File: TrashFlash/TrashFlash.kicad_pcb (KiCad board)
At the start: 2 copper layers, 105 x 45 mm, 113 parts, among them IC1 LTC3643IUDD#PBF, IC10 BQ24230RGTR, IC11 STM32L471QEI6, IC2 ADG5419BCPZ-RL7, IC3 BQ27426YZFR, IC4 SN74LXC2T45QDTTRQ1, IC5 TPS63900DSKR, IC6 TPS63900DSKR, IC7 LP5024RSMR, IC8 AD8615AUJZ-REEL, IC9 BQ29732DSER, J1 USB4800-03-A, Q1 BC56-10PA,115, Q2 BC56-10PA,115, Q3 BC56-10PA,115, Q4 BC56-10PA,115, Q5 PMDPB30XNAX, U1 SI5448DU-T1-GE3, U2 SI5448DU-T1-GE3, Y1 ECS-160-8-33B2-CTN-TR3

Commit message: Added Wireless and inter PCB connector
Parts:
- removed LED1, LED2, LED3, LED4, LED5, LED6, LED7, LED8: 150353M153300, TrashFlash:150353M153300
- added ANT801: 0868AT43A0020001E, TrashFlash:ANTC7020X90N, F.Cu at (276.5, 102.4)
- added C201: 100p, Capacitor_SMD:C_0402_1005Metric, F.Cu at (40.2, 79.1)
- added C202: 100p, Capacitor_SMD:C_0402_1005Metric, F.Cu at (40.2, 81.1)
- added C304: 10u, Capacitor_SMD:C_1206_3216Metric, F.Cu at (40.5, 188.2)
- added C305: 10u, Capacitor_SMD:C_1206_3216Metric, F.Cu at (40.5, 191.5)
- added C801: 1.5p, Capacitor_SMD:C_0402_1005Metric, F.Cu at (264.4, 101.3)
- added C802: 1p, Capacitor_SMD:C_0402_1005Metric, F.Cu at (264.4, 103.3)
- added C803: 100p, Capacitor_SMD:C_0402_1005Metric, F.Cu at (264.4, 105.3)
- added C804: 1.5p, Capacitor_SMD:C_0402_1005Metric, F.Cu at (264.4, 107.2)
- added C805: 3.3p, Capacitor_SMD:C_0402_1005Metric, F.Cu at (264.4, 109.2)
- added C806: 3.9p, Capacitor_SMD:C_0402_1005Metric, F.Cu at (264.4, 111.2)
- added C807: 0.3p, Capacitor_SMD:C_0402_1005Metric, F.Cu at (264.4, 113.2)
- added C808: 10p, Capacitor_SMD:C_0402_1005Metric, F.Cu at (267.2, 101.3)
- added C809: 10p, Capacitor_SMD:C_0402_1005Metric, F.Cu at (267.2, 103.3)
- added C810: 100p, Capacitor_SMD:C_0402_1005Metric, F.Cu at (267.2, 105.3)
- added C811: 100n, Capacitor_SMD:C_0402_1005Metric, F.Cu at (267.2, 107.2)
- added C812: 220p, Capacitor_SMD:C_0402_1005Metric, F.Cu at (267.2, 109.2)
- added C813: 220p, Capacitor_SMD:C_0402_1005Metric, F.Cu at (267.2, 111.2)
- added C814: 10n, Capacitor_SMD:C_0402_1005Metric, F.Cu at (267.2, 113.2)
- added C815: 220p, Capacitor_SMD:C_0402_1005Metric, F.Cu at (270.1, 101.3)
- added C816: 10n, Capacitor_SMD:C_0402_1005Metric, F.Cu at (270.1, 103.3)
- added C817: 100n, Capacitor_SMD:C_0402_1005Metric, F.Cu at (270.1, 105.3)
- added IC801: CC110LRGPR, TrashFlash:QFN50P400X400X100-21N-D, F.Cu at (277.0, 113.8)
- added J101: 15130322601000, TrashFlash:15130322601000, B.Cu at (202.0, 125.0)
- added J102: 15230322601000, TrashFlash:15230322601000, F.Cu at (142.0, 126.0)
- added L801: 12n, Inductor_SMD:L_01005_0402Metric, F.Cu at (272.7, 105.3)
- added L802: 18n, Inductor_SMD:L_01005_0402Metric, F.Cu at (272.7, 107.0)
- added L803: 12n, Inductor_SMD:L_01005_0402Metric, F.Cu at (272.7, 108.6)
- added L804: 12n, Inductor_SMD:L_01005_0402Metric, F.Cu at (272.7, 110.3)
- added L805: 18n, Inductor_SMD:L_01005_0402Metric, F.Cu at (272.7, 111.9)
- added L806: 12n, Inductor_SMD:L_01005_0402Metric, F.Cu at (272.7, 113.6)
- added L807: 18n, Inductor_SMD:L_01005_0402Metric, F.Cu at (272.7, 115.2)
- added LED601: 150282M153310, TrashFlash:150282M153310, F.Cu at (185.0, 155.0)
- added LED602: 150282M153310, TrashFlash:150282M153310, F.Cu at (184.5, 150.5)
- added LED603: 150282M153310, TrashFlash:150282M153310, F.Cu at (183.0, 146.3)
- added LED604: 150282M153310, TrashFlash:150282M153310, F.Cu at (180.6, 142.5)
- added LED605: 150282M153310, TrashFlash:150282M153310, F.Cu at (177.5, 139.4)
- added LED606: 150282M153310, TrashFlash:150282M153310, F.Cu at (173.7, 137.0)
- added LED607: 150282M153310, TrashFlash:150282M153310, F.Cu at (169.5, 135.5)
- added LED608: 150282M153310, TrashFlash:150282M153310, F.Cu at (165.0, 135.0)
- added R201: 100k, Resistor_SMD:R_0402_1005Metric, F.Cu at (37.3, 79.1)
- added R202: 5.1k, Resistor_SMD:R_0402_1005Metric, F.Cu at (37.3, 81.1)
- added R203: 100k, Resistor_SMD:R_0402_1005Metric, F.Cu at (37.3, 83.1)
- added R204: 5.1k, Resistor_SMD:R_0402_1005Metric, F.Cu at (37.3, 85.1)
- added R801: 330, Capacitor_SMD:C_0402_1005Metric, F.Cu at (270.1, 107.2)
- added R802: 56k, Capacitor_SMD:C_0402_1005Metric, F.Cu at (270.1, 109.2)
- added Y801: ECS-260-10-33B-CKM-TR, TrashFlash:ECS160833B2CTNTR3, F.Cu at (277.1, 107.5)
- C303: renamed from C7; value 22u -> 10u; footprint Capacitor_SMD:C_0603_1608Metric -> Capacitor_SMD:C_1206_3216Metric
- D201: renamed from D4; moved to B.Cu
- D202: renamed from D3; moved to B.Cu
- D203: renamed from D2; moved to B.Cu
- D204: renamed from D1; moved to B.Cu
- R205: renamed from R9; value 150k -> 100k
- R206: renamed from R7; value 12k -> 10k
- R211: renamed from R6; value 12k -> 10k
- R212: renamed from R8; value 150k -> 100k
- R213: renamed from R18; footprint Resistor_SMD:R_0603_1608Metric -> Resistor_SMD:R_0805_2012Metric
- R214: renamed from R5; footprint Resistor_SMD:R_0603_1608Metric -> Resistor_SMD:R_0805_2012Metric
- R502: renamed from R23; value 36.5k -> 6.49k
- moved Y401 181.7 mm to (275.3, 128.5)
- moved IC401 171.3 mm to (266.7, 126.2)
- moved IC601 162.3 mm to (265.0, 159.0)
- moved C601 155.9 mm to (276.7, 157.4)
- moved C602 155.9 mm to (276.7, 159.9)
- moved R601 155.9 mm to (273.2, 159.1)
- moved R602 155.9 mm to (273.2, 157.2)
- moved R603 155.9 mm to (273.2, 161.1)
- moved C401 139.6 mm to (273.9, 141.2)
- moved C402 139.6 mm to (267.6, 146.3)
- moved C403 139.6 mm to (273.9, 143.7)
- moved C406 139.6 mm to (273.9, 138.7)
- moved C408 139.6 mm to (264.7, 148.3)
- moved C412 139.6 mm to (264.7, 146.3)
- moved C404 139.6 mm to (264.7, 140.4)
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- renumbered C2 to C203, C1 to C204, C14 to C205, C13 to C206, C12 to C207, C4 to C208, C3 to C209, C5 to C301, C6 to C302, C8 to C306, C9 to C307, C10 to C308, C11 to C309, C35 to C401, C36 to C402, C37 to C403, C25 to C404, C24 to C405, C34 to C406, C26 to C407, C29 to C408, C31 to C409, C27 to C410, C33 to C411, C28 to C412, C30 to C413, C32 to C414, C15 to C501, C16 to C502, C17 to C503, C18 to C504, C19 to C601, C20 to C602, C22 to C701, C21 to C702, C23 to C703, IC8 to IC201, IC2 to IC202, IC4 to IC203, IC1 to IC301, IC11 to IC401, IC5 to IC501, IC6 to IC502, IC7 to IC601, IC3 to IC701, IC10 to IC702, IC9 to IC703, J1 to J701, L1 to L301, L4 to L501, L5 to L502, Q4 to Q201, Q3 to Q202, Q2 to Q203, Q1 to Q204, Q5 to Q701, R1 to R207, R2 to R208, R3 to R209, R4 to R210, R20 to R215, R19 to R216, R10 to R301, R14 to R302, R17 to R303, R15 to R304, R16 to R305, R43 to R401, R41 to R402, R42 to R403, R40 to R404, R22 to R501, R24 to R503, R25 to R504, R26 to R505, R28 to R601, R27 to R602, R29 to R603, R30 to R701, R32 to R702, R31 to R703, R36 to R704, R37 to R705, R33 to R706, R34 to R707, R35 to R708, R38 to R709, R39 to R710, S1 to S601, U2 to U201, U1 to U202, Y1 to Y401
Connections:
- net /User_Interface/EN_RGB_LED_DRIVER renamed /MCU/EN_RGB_LED_DRIVER
- net /User_Interface/SCL renamed /MCU/SCL_USER_INTERFACE
- net /User_Interface/SDA renamed /MCU/SDA_USER_INTERFACE
- IC501 pad 2: /Supply/SELECT_VDD -> VSYS
- IC501 pad 5: /Supply/CFG3_VDD -> GND
- S601 pad 1: unconnected-(S1-A-Pad1) -> /MCU/ENCODER_A
- S601 pad 2: unconnected-(S1-C-Pad2) -> GND
- S601 pad 3: unconnected-(S1-B-Pad3) -> /MCU/ENCODER_B
- S601 pad 4: unconnected-(S1-D-Pad4) -> /MCU/PUSH_BUTTON
- S601 pad 5: unconnected-(S1-E-Pad5) -> GND
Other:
- board size 105 x 45 mm -> 108 x 60 mm

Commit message: Added battery and connectors to PCB
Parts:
- added BT1: 628, TrashFlash:BAT_628, F.Cu at (106.0, 150.0)
- added BT2: 5223, TrashFlash:BAT_5223, F.Cu at (151.5, 149.5)
- added REF**: CR123A, TrashFlash:CR123A, F.Cu at (128.0, 150.0)
- moved C304 47.1 mm to (87.0, 180.7)
- moved C305 47.1 mm to (87.0, 184.0)
- moved L301 47.1 mm to (95.5, 193.0)
- moved C301 47.1 mm to (97.3, 178.5)
- moved C302 47.1 mm to (100.8, 178.2)
- moved C303 47.1 mm to (97.3, 181.0)
- moved C307 47.1 mm to (100.8, 180.2)
- moved C308 47.1 mm to (100.8, 182.2)
- moved C309 47.1 mm to (97.3, 183.5)
- moved R301 47.1 mm to (97.3, 186.0)
- moved R302 47.1 mm to (92.5, 179.5)
- moved R303 47.1 mm to (92.5, 185.5)
- moved R304 47.1 mm to (92.5, 181.5)
- moved R305 47.1 mm to (92.5, 183.5)
- moved IC301 46.6 mm to (86.0, 191.8)
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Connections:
- net /SELECT_VDD renamed /SELECT_VDD_1

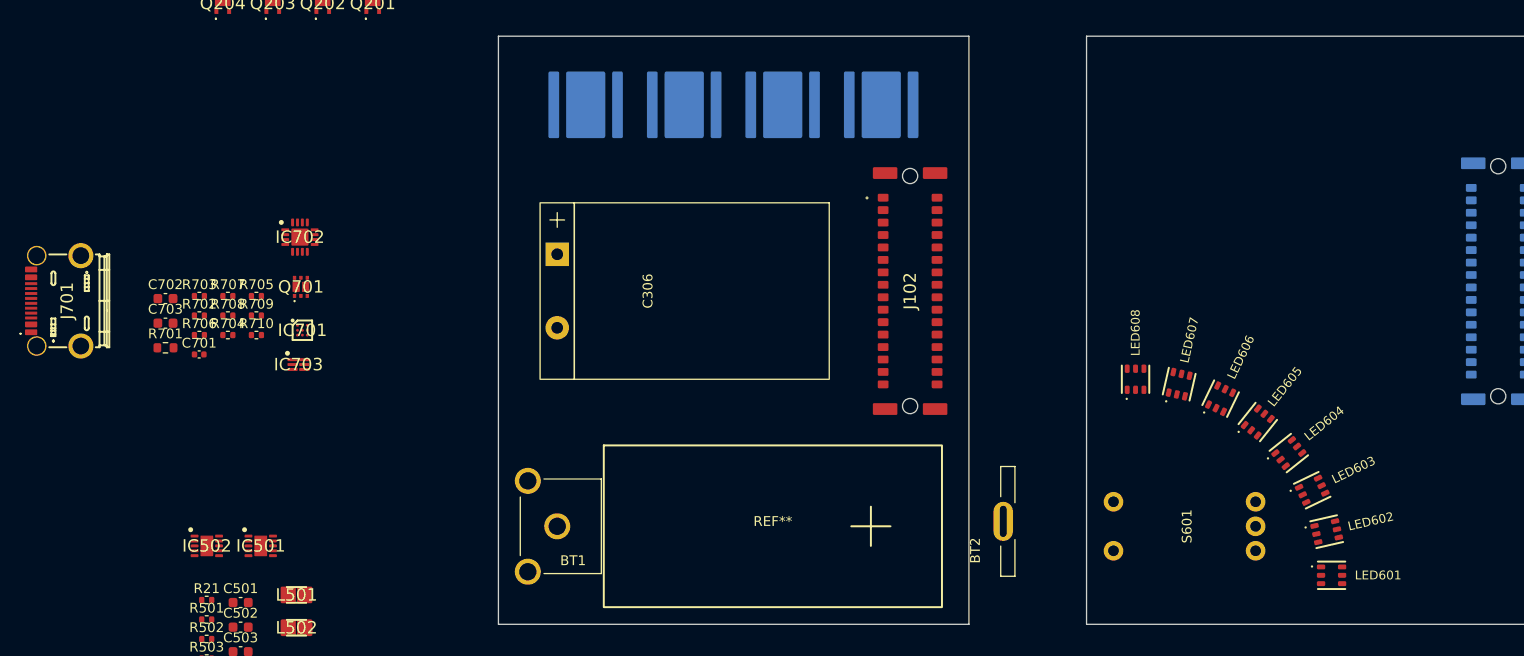
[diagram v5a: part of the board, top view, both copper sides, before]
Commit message: Stackup changed, Led placement adjusted
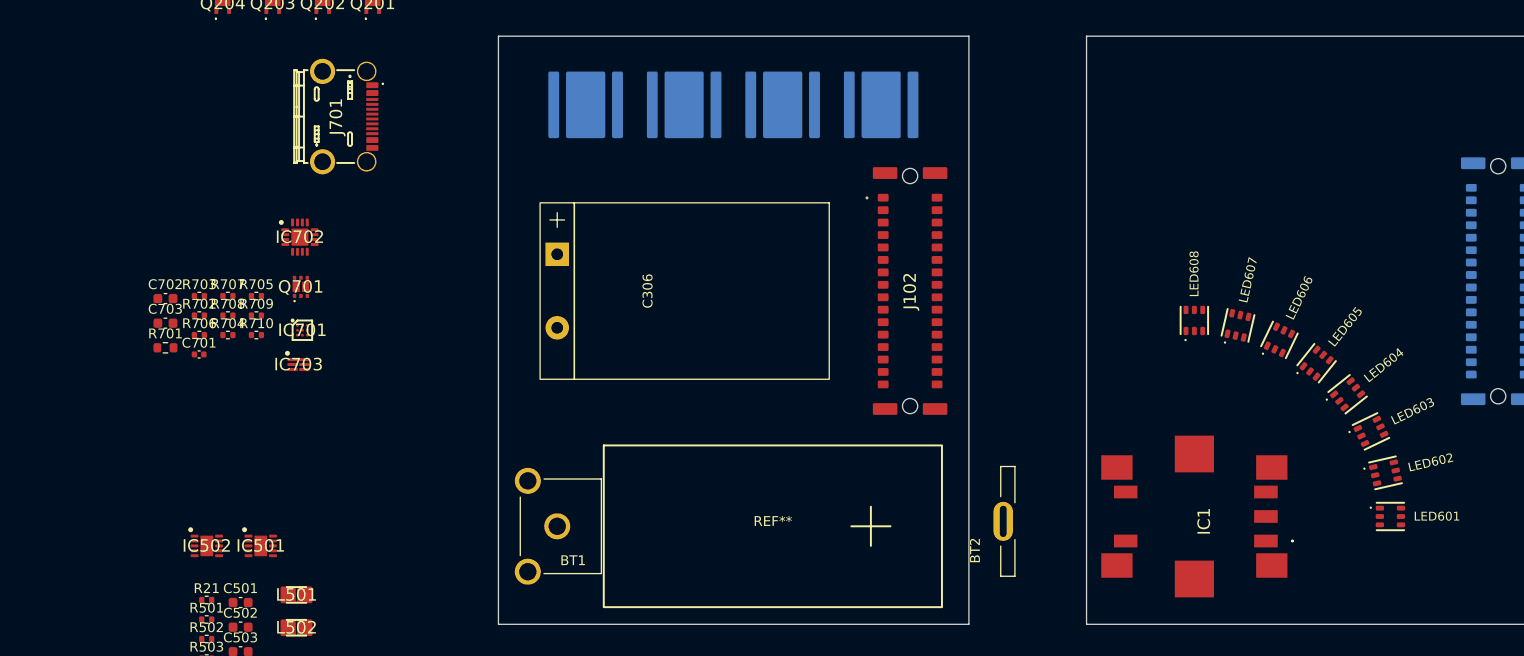
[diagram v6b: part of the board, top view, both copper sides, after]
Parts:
- removed the LED608 at (165.0, 135.0)
- removed S601: ec11e09244aq, TrashFlash:ec11e09244aq
- added IC1: PEC11S-929K-S0015, TrashFlash:PEC11S929KS0015, F.Cu at (171.0, 149.0)
- added LED601: 150282M153310, TrashFlash:150282M153310, F.Cu at (191.0, 149.0)
- moved J701 33.3 mm to (83.5, 108.2), turned to -90 degrees
- moved LED608 29.5 mm to (171.0, 129.0), turned to 89.999 degrees
- moved LED607 8.49 mm to (175.5, 129.5)
- moved LED606 8.49 mm to (179.7, 131.0)
- moved LED605 8.49 mm to (183.5, 133.4)
- moved LED604 8.49 mm to (186.6, 136.5)
- moved LED602 8.49 mm to (190.5, 144.5)
- moved LED603 8.49 mm to (189.0, 140.3)
- renumbered LED601 to LED608
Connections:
- LED608 pad 1: /User_Interface/RED0 -> /User_Interface/RED7
- LED608 pad 2: /User_Interface/GREEN0 -> /User_Interface/GREEN7
- LED608 pad 3: /User_Interface/BLUE0 -> /User_Interface/BLUE7
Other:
- copper layers 2 -> 6

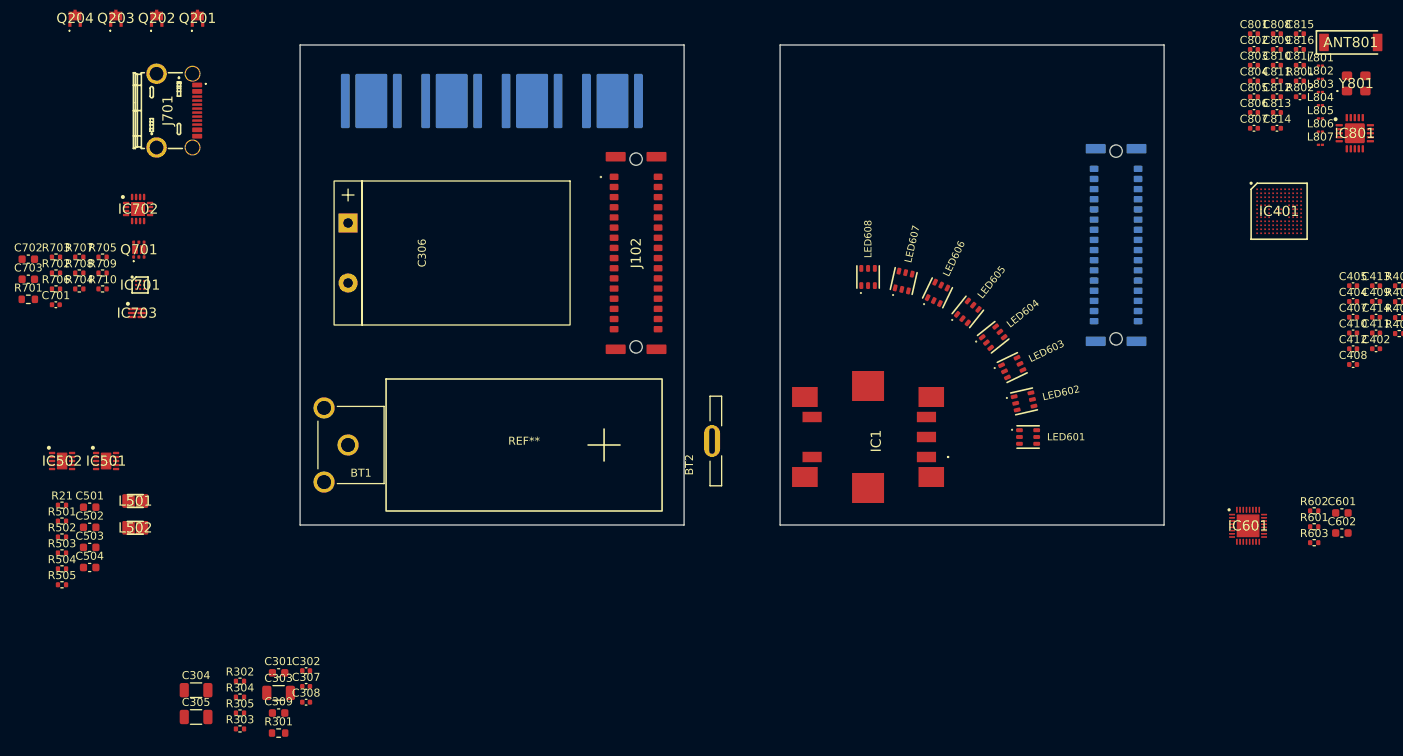
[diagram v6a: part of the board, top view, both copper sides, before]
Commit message: Moved USB and added JTAG connector
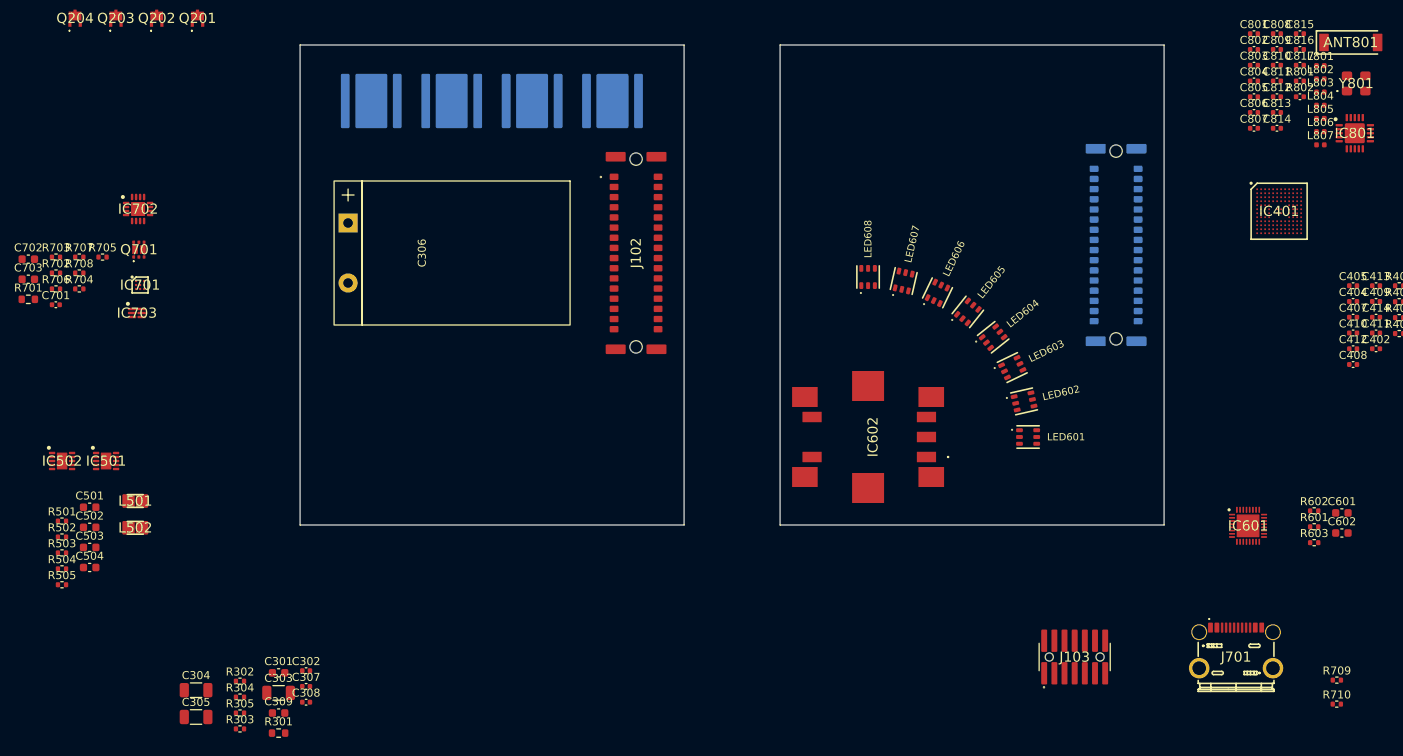
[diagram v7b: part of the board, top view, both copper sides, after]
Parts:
- removed BT1: 628, TrashFlash:BAT_628
- removed BT2: 5223, TrashFlash:BAT_5223
- removed IC1: PEC11S-929K-S0015, TrashFlash:PEC11S929KS0015
- removed R21: 0, Resistor_SMD:R_0402_1005Metric
- removed REF**: CR123A, TrashFlash:CR123A
- added IC602: PEC11S-929K-S0015, TrashFlash:PEC11S929KS0015, F.Cu at (171.0, 149.0)
- added J103: FTSH-107-01-L-DV-K-A, TrashFlash:FTSH-107-XX-YYY-DV-K-A, F.Cu at (196.8, 176.5)
- L801, L802, L803, L804, L805, L806, L807: footprint Inductor_SMD:L_01005_0402Metric -> Inductor_SMD:L_0402_1005Metric
- moved R710 162.8 mm to (229.6, 182.4)
- moved R709 162.5 mm to (229.6, 179.4)
- moved J701 150.0 mm to (217.0, 176.5), turned to 0 degrees
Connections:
- net /Battery_Management/CC1 renamed /CC1
- net /Battery_Management/CC2 renamed /CC2
- net /SELECT_VDD_1 renamed /SELECT_VDD
- J101 pad A10: /MCU/USB_DN -> /MCU/~{CHG}
- J101 pad A11: /MCU/~{CHG} -> unconnected-(J101-PadA11)
- J101 pad A13: unconnected-(J101-PadA13) -> VBUS
- J101 pad B10: /MCU/USB_DP -> /MCU/~{PGOOD}
- J101 pad B11: /MCU/~{PGOOD} -> unconnected-(J101-PadB11)
- J101 pad B13: unconnected-(J101-PadB13) -> VBUS
- J102 pad A10: /Battery_Management/USB_DN -> /Battery_Management/~{CHG}
- J102 pad A11: /Battery_Management/~{CHG} -> unconnected-(J102-PadA11)
- J102 pad A13: unconnected-(J102-PadA13) -> VBUS
- J102 pad A14: VDD -> +5V
- J102 pad A15: +5V -> VDD
- J102 pad B10: /Battery_Management/USB_DP -> /Battery_Management/~{PGOOD}
- J102 pad B11: /Battery_Management/~{PGOOD} -> unconnected-(J102-PadB11)
- J102 pad B13: unconnected-(J102-PadB13) -> VBUS
- J102 pad B14: VDD -> +5V
- J102 pad B15: +5V -> VDD
- J701 pad A6: /Battery_Management/USB_DP -> /MCU/USB_DP
- J701 pad A7: /Battery_Management/USB_DN -> /MCU/USB_DN
- J701 pad B6: /Battery_Management/USB_DP -> /MCU/USB_DP
- J701 pad B7: /Battery_Management/USB_DN -> /MCU/USB_DN
